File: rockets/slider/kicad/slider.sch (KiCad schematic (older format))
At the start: 40 parts, among them J1 I2C Breakout, J2 SPI Breakout, J4 Pyro 1 Terminal, M1 Servo X, M2 Servo Y, Q1 IRF540N, Q2 IRF540N, Q3 IRF540N, SW1 SW_SPDT, SW2 SW_SPDT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

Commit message: Lots of 3d models for kicad and rethinking the pcb design
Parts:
- A1: footprint (none) -> slider:Adafruit-BNO055
- A2: footprint (none) -> slider:Adafruit-BMP280
- A3: footprint (none) -> slider:Adafruit-MB85RC256V
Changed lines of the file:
@@
 F 0 "A3" H 13300 7365 50  0000 C CNN
 F 1 "MB85RC256V" H 13300 7274 50  0000 C CNN
-F 2 "" H 13300 6900 50  0001 C CNN
+F 2 "slider:Adafruit-MB85RC256V" H 13300 6900 50  0001 C CNN
 F 3 "https://learn.adafruit.com/adafruit-i2c-fram-breakout/overview" H 13300 6900 50  0001 C CNN
 	1    13300 6900
@@
 F 0 "A2" H 11300 8050 50  0000 C CNN
 F 1 "Adafruit-BMP280" V 11400 7600 50  0000 C CNN
-F 2 "" H 11200 7700 50  0001 C CNN
+F 2 "slider:Adafruit-BMP280" H 11200 7700 50  0001 C CNN
 F 3 "https://learn.adafruit.com/adafruit-bmp280-barometric-pressure-plus-temperature-sensor-breakout/overview" H 11200 7700 50  0001 C CNN
 	1    11300 7600
@@
 F 0 "A1" H 13300 8200 50  0000 C CNN
 F 1 "Adafruit-BNO055" H 13300 7400 50  0000 C CNN
-F 2 "" H 13550 7500 50  0001 C CNN
+F 2 "slider:Adafruit-BNO055" H 13550 7500 50  0001 C CNN
 F 3 "https://learn.adafruit.com/adafruit-bno055-absolute-orientation-sensor/overview" H 13550 7500 50  0001 C CNN
 	1    13300 7800

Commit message: Near v1 of board layout
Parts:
- removed A3: MB85RC256V, slider:Adafruit-MB85RC256V, symbol slider:MB85RC256V
- removed BZ1: Alarm Buzzer, slider:CE-C75-Piezo-Alarm, symbol Device:Buzzer
- removed J1: I2C Breakout, Connector_PinHeader_2.54mm:PinHeader_1x04_P2.54mm_Vertical, symbol Connector:Conn_01x04_Male
- removed J2: SPI Breakout, Connector_PinHeader_2.54mm:PinHeader_1x05_P2.54mm_Vertical, symbol Connector:Conn_01x05_Male
- removed J4: Pyro 1 Terminal, TerminalBlock_4Ucon:TerminalBlock_4Ucon_1x02_P3.50mm_Horizontal, symbol Connector:Screw_Terminal_01x02
- removed Q2, Q3: IRF540N, Package_TO_SOT_THT:TO-220-3_Vertical, symbol Transistor_FET:IRF540N
- removed R10, R12: 2.2k, Resistor_THT:R_Axial_DIN0207_L6.3mm_D2.5mm_P7.62mm_Horizontal, symbol Device:R
- removed R11, R9: 220, Resistor_THT:R_Axial_DIN0207_L6.3mm_D2.5mm_P7.62mm_Horizontal, symbol Device:R
- removed R13: 220k, Resistor_THT:R_Axial_DIN0207_L6.3mm_D2.5mm_P7.62mm_Horizontal, symbol Device:R
- removed R14: 100k, Resistor_THT:R_Axial_DIN0207_L6.3mm_D2.5mm_P7.62mm_Horizontal, symbol Device:R
- removed SW2: SW_SPDT, symbol Switch:SW_SPDT
- added D2: LED (RED), LED_THT:LED_D5.0mm, symbol Device:LED
- added D3: D_Schottky, Diode_THT:D_DO-35_SOD27_P7.62mm_Horizontal, symbol Device:D_Schottky
- added J1: Parachute, Connector_PinHeader_2.54mm:PinHeader_1x03_P2.54mm_Vertical, symbol Connector:Conn_01x03_Male
- added R4: 220, Resistor_THT:R_Axial_DIN0207_L6.3mm_D2.5mm_P7.62mm_Horizontal, symbol Device:R
- added U5: FM25V20A-PG, cypress:FM25V20A, symbol cypress:FM25V20A-PG
- A1: value Adafruit-BNO055 -> BNO055; footprint slider:Adafruit-BNO055 -> adafruit:Adafruit_BNO055; symbol slider:Adafruit-BNO055 -> adafruit:Adafruit-BNO055
- A2: value Adafruit-BMP280 -> BMP280; footprint slider:Adafruit-BMP280 -> adafruit:Adafruit_BMP280; symbol slider:Adafruit-BMP280 -> adafruit:Adafruit-BMP280
- D1: value LED (RED) -> LED (YLO)
- LS1: footprint Sparkfun Electromechanical:BUZZER-12MM -> SparkFun-Electromechanical:BUZZER-12MM
- SW1: footprint (none) -> digikey-footprints:Switch_Toggle_ATE1D-2M3-10-Z
- U4: footprint RPi_Pico:RPi_Pico_TH_Perfboard -> MCU_RaspberryPi_and_Boards:RPi_Pico_TH_Perfboard
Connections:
- net +3V3: now also U5.3 (WP), U5.8 (VDD)
- net +BATT: now also D3.1 (K), J1.1 (Pin_1)
- net ARM: now also U4.10 (GPIO7), D2.2 (A); no longer U4.20 (GPIO15)
- net Alarm_EN: no longer U4.19 (GPIO14)
- net BMP280_CS: now also U4.27 (GPIO21); no longer U4.22 (GPIO17)
- net GND: now also J1.3 (Pin_3), R4.1, U5.4 (VSS)
- net PWM_Buzzer: now also U4.20 (GPIO15); no longer U4.17 (GPIO13)
- net PWM_Servo_X: now also U4.14 (GPIO10); no longer U4.27 (GPIO21)
- net PWM_Servo_Z: now also U4.15 (GPIO11); no longer U4.26 (GPIO20)
- net Pyro_1: no longer U4.14 (GPIO10)
- net Pyro_1_Cont: no longer U4.15 (GPIO11)
- net SPI0_RX: now also U5.2 (SO)
- net SPI0_SCK: now also U5.6 (SCK)
- net SPI0_TX: now also U5.5 (SI)
- net Servo_EN: now also U4.12 (GPIO9); no longer U4.29 (GPIO22)
- net at BT1.1 (+): now also D3.2 (A)
- new net: D2.1 (K), R4.2
- new net FRAM_CS: U4.26 (GPIO20), U5.1 (CS)
- new net Parachute_Deploy: J1.2 (Pin_2), U4.29 (GPIO22)
- no-connect marks 24 -> 26
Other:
- note added: "ADC Connections:\n3: (Internal) Temperature Sensor\n2: Battery voltage divider\n\n1: Ground reference\n0:"
- note added: "DISABLED"
- note added: "I2C FRAM"
- note added: "I2C IMU"
- note added: "Parachute"
- note added: "SPI Barom"
- note added: "SPI FRAM"
- note removed: "ADC Connections:\n3: (Internal) Temperature Sensor\n2: Battery voltage divider\n1: Ground reference\n0:"
- moved on the sheet: A2, D5, LS1, M1, M2, NT1, S1, SW1, U4

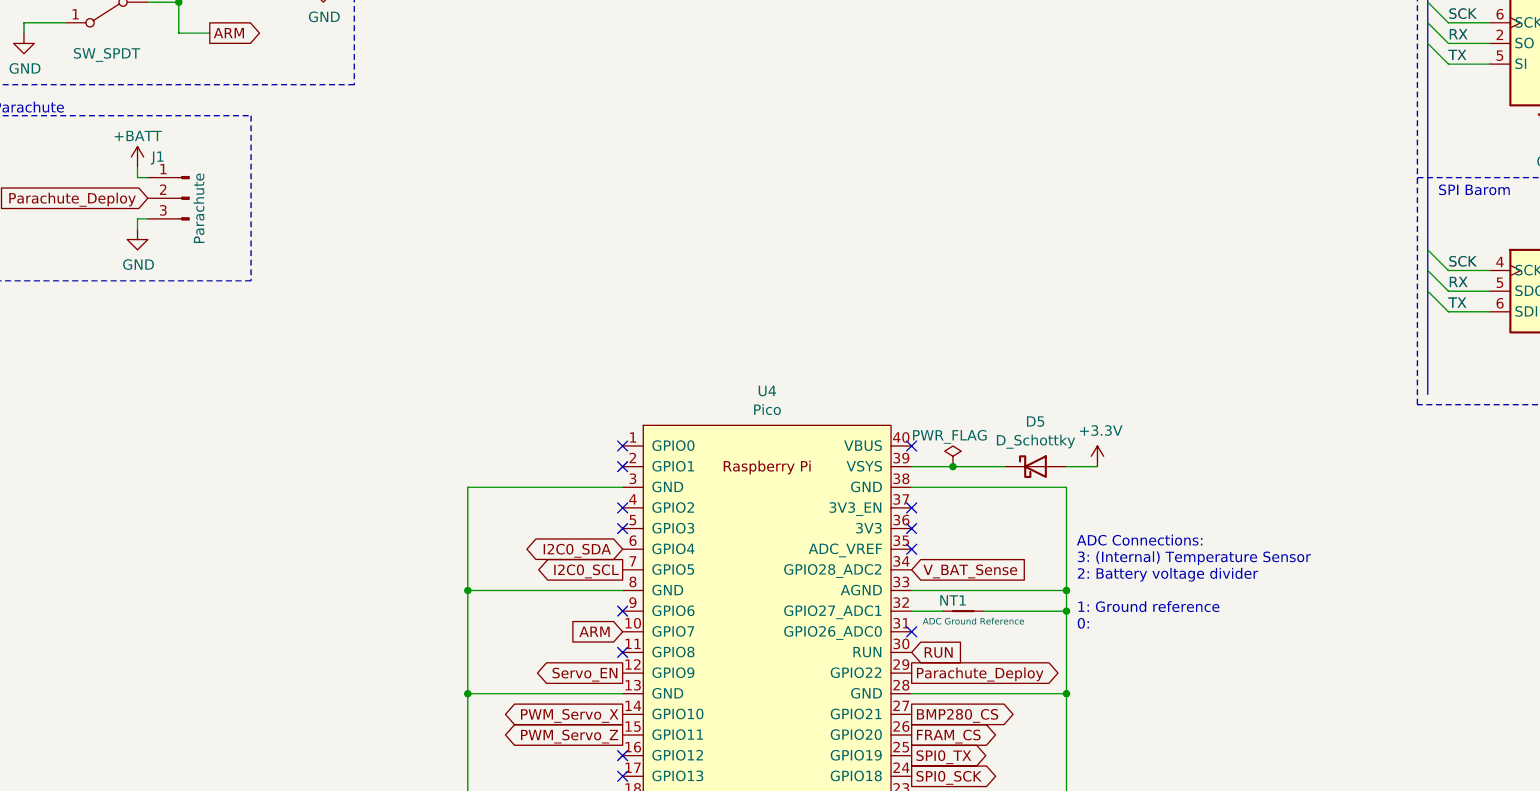
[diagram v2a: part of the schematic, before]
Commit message: Routing and an additional pin header
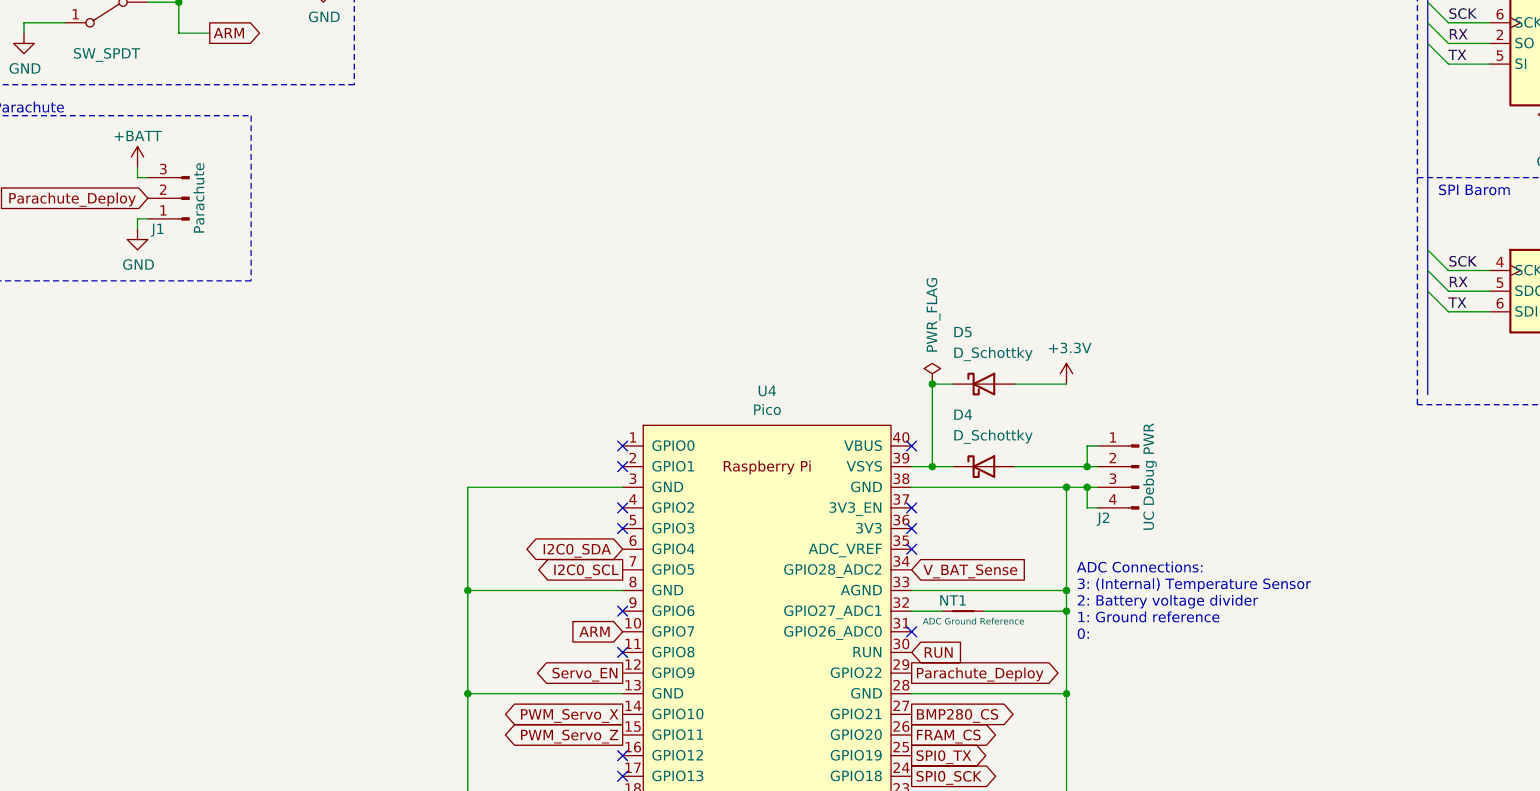
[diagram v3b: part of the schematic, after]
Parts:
- added D4: D_Schottky, Diode_THT:D_DO-35_SOD27_P7.62mm_Horizontal, symbol Device:D_Schottky
- added J2: UC Debug PWR, Connector_PinHeader_2.54mm:PinHeader_1x04_P2.54mm_Vertical, symbol Connector:Conn_01x04_Male
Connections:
- net +BATT: now also J1.3 (Pin_3); no longer J1.1 (Pin_1)
- net GND: now also J1.1 (Pin_1), J2.3 (Pin_3), J2.4 (Pin_4); no longer J1.3 (Pin_3)
- net at D5.1 (K), U4.39 (VSYS): now also D4.1 (K)
- new net: D4.2 (A), J2.1 (Pin_1), J2.2 (Pin_2)
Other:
- note added: "ADC Connections:\n3: (Internal) Temperature Sensor\n2: Battery voltage divider\n1: Ground reference\n0:"
- note removed: "ADC Connections:\n3: (Internal) Temperature Sensor\n2: Battery voltage divider\n\n1: Ground reference\n0:"
- moved on the sheet: D5
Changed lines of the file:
@@
 NoConn ~ 9000 5200
 NoConn ~ 9000 5400
-$Comp
-L power:GND #PWR022
-U 1 1 606B9AD8
-P 8300 7100
-F 0 "#PWR022" H 8300 6850 50  0001 C CNN
-F 1 "GND" H 8305 6927 50  0000 C CNN
-F 2 "" H 8300 7100 50  0001 C CNN
-F 3 "" H 8300 7100 50  0001 C CNN
-	1    8300 7100
-	1    0    0    -1
-$EndComp
-Wire Wire Line
-	9750 7100 9750 6600
-Wire Wire Line
-	9750 6600 9000 6600
-Wire Wire Line
-	9000 6100 9750 6100
-Wire Wire Line
-	9750 6100 9750 6600
-Connection ~ 9750 6600
-Wire Wire Line
-	9750 5600 9750 5700
-Connection ~ 9750 6100
-Wire Wire Line
-	9000 5100 9750 5100
-Wire Wire Line
-	9750 5100 9750 5600
-Connection ~ 9750 5600
-Wire Wire Line
-	6850 5100 6850 5600
-Wire Wire Line
-	7600 6100 6850 6100
-Connection ~ 6850 6100
-Wire Wire Line
-	7600 5600 6850 5600
-Connection ~ 6850 5600
-Wire Wire Line
-	6850 5600 6850 6100
-Wire Wire Line
-	6850 5100 7600 5100
 Text GLabel 7600 6300 0    50   Output ~ 0
 PWM_Servo_Z
@@
 Wire Wire Line
 	9000 5700 9150 5700
-Text Notes 9800 5800 0    50   ~ 0
-ADC Connections:\n3: (Internal) Temperature Sensor\n2: Battery voltage divider\n\n1: Ground reference\n0:
 $Comp
 L power:+3.3V #PWR023
 U 1 1 6071506B
-P 9900 5000
-F 0 "#PWR023" H 9900 4850 50  0001 C CNN
-F 1 "+3.3V" H 9915 5173 50  0000 C CNN
-F 2 "" H 9900 5000 50  0001 C CNN
-F 3 "" H 9900 5000 50  0001 C CNN
-	1    9900 5000
+P 9750 4600
+F 0 "#PWR023" H 9750 4450 50  0001 C CNN
+F 1 "+3.3V" H 9765 4773 50  0000 C CNN
+F 2 "" H 9750 4600 50  0001 C CNN
+F 3 "" H 9750 4600 50  0001 C CNN
+	1    9750 4600
 	1    0    0    -1
 $EndComp
@@
 Text GLabel 7600 6800 0    50   Output ~ 0
 PWM_Buzzer
-Wire Wire Line
-	7600 6600 6850 6600
-Wire Wire Line
-	6850 6100 6850 6600
-Wire Wire Line
-	6850 6600 6850 7100
-Connection ~ 6850 6600
 $Comp
 L power:+3.3V #PWR013
@@
 Wire Wire Line
 	1250 5150 1900 5150
-$Comp
-L Device:Net-Tie_2 NT1
-U 1 1 608A8144
-P 9250 5700
-F 0 "NT1" H 9300 5650 50  0000 C CNN
-F 1 "ADC Ground Reference" H 9200 5750 31  0000 C CNN
-F 2 "NetTie:NetTie-2_SMD_Pad0.5mm" H 9250 5700 50  0001 C CNN
-F 3 "~" H 9250 5700 50  0001 C CNN
-	1    9250 5700
-	-1   0    0    1
-$EndComp
-Wire Wire Line
-	9000 5600 9750 5600
-Wire Wire Line
-	9350 5700 9750 5700
-Connection ~ 9750 5700
-Wire Wire Line
-	9750 5700 9750 6100
-Wire Wire Line
-	9900 5000 9750 5000
-$Comp
-L Device:D_Schottky D5
-U 1 1 6070DD54
-P 9600 5000
-F 0 "D5" H 9600 5217 50  0000 C CNN
-F 1 "D_Schottky" H 9600 5126 50  0000 C CNN
-F 2 "Diode_THT:D_DO-35_SOD27_P7.62mm_Horizontal" H 9600 5000 50  0001 C CNN
-F 3 "~" H 9600 5000 50  0001 C CNN
-	1    9600 5000
-	1    0    0    -1
-$EndComp
-Wire Wire Line
-	9200 5000 9000 5000
-Wire Wire Line
-	9450 5000 9200 5000
-Connection ~ 9200 5000
+Wire Wire Line
+	9200 5000 9100 5000
 $Comp
 L dk_Tactile-Switches:1825910-6 S1
@@
 L power:PWR_FLAG #FLG0103
 U 1 1 609192AA
-P 9200 5000
-F 0 "#FLG0103" H 9200 5075 50  0001 C CNN
-F 1 "PWR_FLAG" H 9000 5150 50  0000 L CNN
-F 2 "" H 9200 5000 50  0001 C CNN
-F 3 "~" H 9200 5000 50  0001 C CNN
-	1    9200 5000
+P 9100 4600
+F 0 "#FLG0103" H 9100 4675 50  0001 C CNN
+F 1 "PWR_FLAG" V 9100 4750 50  0000 L CNN
+F 2 "" H 9100 4600 50  0001 C CNN
+F 3 "~" H 9100 4600 50  0001 C CNN
+	1    9100 4600
 	1    0    0    -1
 $EndComp
@@
 	1    0    0    -1
 $EndComp
-Wire Wire Line
-	6850 7100 8300 7100
-Wire Wire Line
-	8300 7100 9750 7100
-Connection ~ 8300 7100
 Wire Wire Line
 	4900 2650 4700 2650
@@
 	1    5650 2600
 	-1   0    0    1
-$EndComp
-$Comp
-L Connector:Conn_01x03_Male J1
-U 1 1 613D5FF7
-P 5500 3700
-F 0 "J1" H 5650 3900 50  0000 C CNN
-F 1 "Parachute" V 5450 3650 50  0000 C CNN
-F 2 "Connector_PinHeader_2.54mm:PinHeader_1x03_P2.54mm_Vertical" H 5500 3700 50  0001 C CNN
-F 3 "~" H 5500 3700 50  0001 C CNN
-	1    5500 3700
-	-1   0    0    -1
 $EndComp
 $Comp
@@
 NoConn ~ 7600 6700
 NoConn ~ 3850 2000
-Wire Bus Line
-	13800 1000 13800 4650
-Wire Bus Line
-	11500 1000 11500 4650
 $Comp
 L Device:D_Schottky D3
@@
 Wire Wire Line
 	1300 4550 1900 4550
+$Comp
+L Device:D_Schottky D5
+U 1 1 6070DD54
+P 9350 4600
+F 0 "D5" H 9200 4850 50  0000 L CNN
+F 1 "D_Schottky" H 9200 4750 50  0000 L CNN
+F 2 "Diode_THT:D_DO-35_SOD27_P7.62mm_Horizontal" H 9350 4600 50  0001 C CNN
+F 3 "~" H 9350 4600 50  0001 C CNN
+	1    9350 4600
+	1    0    0    -1
+$EndComp
+Wire Wire Line
+	9100 5000 9100 4600
+Wire Wire Line
+	9100 4600 9200 4600
+Connection ~ 9100 5000
+Wire Wire Line
+	9500 4600 9750 4600
+Connection ~ 9100 4600
+Wire Wire Line
+	9000 5000 9100 5000
+$Comp
+L Device:D_Schottky D4
+U 1 1 60D2E50B
+P 9350 5000
+F 0 "D4" H 9200 5250 50  0000 L CNN
+F 1 "D_Schottky" H 9200 5150 50  0000 L CNN
+F 2 "Diode_THT:D_DO-35_SOD27_P7.62mm_Horizontal" H 9350 5000 50  0001 C CNN
+F 3 "~" H 9350 5000 50  0001 C CNN
+	1    9350 5000
+	1    0    0    -1
+$EndComp
+$Comp
+L Connector:Conn_01x03_Male J1
+U 1 1 613D5FF7
+P 5500 3700
+F 0 "J1" H 5650 3850 50  0000 C CNN
+F 1 "Parachute" V 5450 3700 50  0000 C CNN
+F 2 "Connector_PinHeader_2.54mm:PinHeader_1x03_P2.54mm_Vertical" H 5500 3700 50  0001 C CNN
+F 3 "~" H 5500 3700 50  0001 C CNN
+	1    5500 3700
+	-1   0    0    1
+$EndComp
+Wire Wire Line
+	9500 5000 9850 5000
+Wire Wire Line
+	9850 5000 9850 4900
+Wire Wire Line
+	9850 4900 9900 4900
+Connection ~ 9850 5000
+Wire Wire Line
+	9850 5000 9900 5000
+Wire Wire Line
+	9850 5100 9850 5200
+Wire Wire Line
+	9850 5200 9900 5200
+Wire Wire Line
+	9850 5100 9900 5100
+Text Notes 9800 5850 0    50   ~ 0
+ADC Connections:\n3: (Internal) Temperature Sensor\n2: Battery voltage divider\n1: Ground reference\n0:
+$Comp
+L Device:Net-Tie_2 NT1
+U 1 1 608A8144
+P 9250 5700
+F 0 "NT1" H 9300 5650 50  0000 C CNN
+F 1 "ADC Ground Reference" H 9200 5750 31  0000 C CNN
+F 2 "NetTie:NetTie-2_SMD_Pad0.5mm" H 9250 5700 50  0001 C CNN
+F 3 "~" H 9250 5700 50  0001 C CNN
+	1    9250 5700
+	-1   0    0    1
+$EndComp
+Wire Wire Line
+	9750 7100 9750 6600
+Connection ~ 9750 6600
+Wire Wire Line
+	9750 6600 9000 6600
+Wire Wire Line
+	9750 6100 9750 6600
+Connection ~ 9750 6100
+Wire Wire Line
+	9000 6100 9750 6100
+Wire Wire Line
+	9750 5700 9750 6100
+Connection ~ 9750 5700
+Wire Wire Line
+	9350 5700 9750 5700
+Wire Wire Line
+	9750 5100 9750 5600
+Wire Wire Line
+	9750 5600 9750 5700
+Connection ~ 9750 5600
+Wire Wire Line
+	9000 5600 9750 5600
+Connection ~ 9850 5100
+Wire Wire Line
+	9750 5100 9850 5100
+Connection ~ 9750 5100
+Wire Wire Line
+	9000 5100 9750 5100
+Connection ~ 8300 7100
+Wire Wire Line
+	8300 7100 9750 7100
+Wire Wire Line
+	6850 7100 8300 7100
+Wire Bus Line
+	11500 1000 11500 4650
+Wire Bus Line
+	13800 1000 13800 4650
+Wire Wire Line
+	6850 5100 7600 5100
+Wire Wire Line
+	6850 5100 6850 5600
+Connection ~ 6850 5600
+Wire Wire Line
+	7600 5600 6850 5600
+Wire Wire Line
+	6850 5600 6850 6100
+Connection ~ 6850 6100
+Wire Wire Line
+	7600 6100 6850 6100
+Wire Wire Line
+	6850 6600 6850 7100
+Wire Wire Line
+	6850 6100 6850 6600
+Connection ~ 6850 6600
+Wire Wire Line
+	7600 6600 6850 6600
+$Comp
+L power:GND #PWR022
+U 1 1 606B9AD8
+P 8300 7100
+F 0 "#PWR022" H 8300 6850 50  0001 C CNN
+F 1 "GND" H 8305 6927 50  0000 C CNN
+F 2 "" H 8300 7100 50  0001 C CNN
+F 3 "" H 8300 7100 50  0001 C CNN
+	1    8300 7100
+	1    0    0    -1
+$EndComp
+$Comp
+L Connector:Conn_01x04_Male J2
+U 1 1 60D36276
+P 10100 5000
+F 0 "J2" H 10300 4750 50  0000 R CNN
+F 1 "UC Debug PWR" V 10050 4950 50  0000 C CNN
+F 2 "Connector_PinHeader_2.54mm:PinHeader_1x04_P2.54mm_Vertical" H 10100 5000 50  0001 C CNN
+F 3 "~" H 10100 5000 50  0001 C CNN
+	1    10100 5000
+	-1   0    0    -1
+$EndComp
 $EndSCHEMATC
